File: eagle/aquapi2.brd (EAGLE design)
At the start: 102.5 x 80 mm, 5 parts, among them IC1 RASPBERRY_PI_ZERO_W__V1.3_

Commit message: schemtic added
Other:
- board size 102.5 x 80 mm -> 140.5 x 80 mm
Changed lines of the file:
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@@
 <board>
 <plain>
-<wire x1="0" y1="0" x2="102.54" y2="0" width="0" layer="20"/>
-<wire x1="102.54" y1="0" x2="102.54" y2="80" width="0" layer="20"/>
-<wire x1="102.54" y1="80" x2="0" y2="80" width="0" layer="20"/>
+<wire x1="0" y1="0" x2="140.54" y2="0" width="0" layer="20"/>
+<wire x1="140.54" y1="0" x2="140.54" y2="80" width="0" layer="20"/>
+<wire x1="140.54" y1="80" x2="0" y2="80" width="0" layer="20"/>
 <wire x1="0" y1="80" x2="0" y2="0" width="0" layer="20"/>
 </plain>

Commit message: arudino device lib fixed
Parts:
- added R1, R2, R3, RDIV1: 10k, rcl:R0805
- added RDIV2: 16K, rcl:R0805
- added TR1, TR2, TR3: 10k, discrete:RS-2,5
- moved U$2 29.2 mm to (60.0, 33.0)
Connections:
- net RAW renamed N$4
- new net ARD_RX: IC1.8
- new net ARD_TX: RDIV1.2
- new net N$1: R2.2, TR1.2
- new net N$10: U$2.TX0-1
- new net N$13: U$2.GND
- new net N$14: U$2.GND4
- new net N$15: U$2.DTR
- new net N$2: R1.2, TR2.2
- new net N$3: R3.2, TR3.2
- new net N$5: U$2.A7
- new net N$6: U$2.D9
- new net N$7: U$2.A4
- new net N$8: U$2.TX0
- new net N$9: U$2.RX1
- new net RPI_RX: IC1.10, RDIV1.1, RDIV2.2
- new net THERM1: TR1.1, U$2.A1
- new net THERM2: TR2.1, U$2.A2
- new net THERM3: TR3.1, U$2.A3
- net +5V: now also U$2.VCC1
- net GND: now also R1.1, R2.1, R3.1, RDIV2.1; no longer U$2.GND

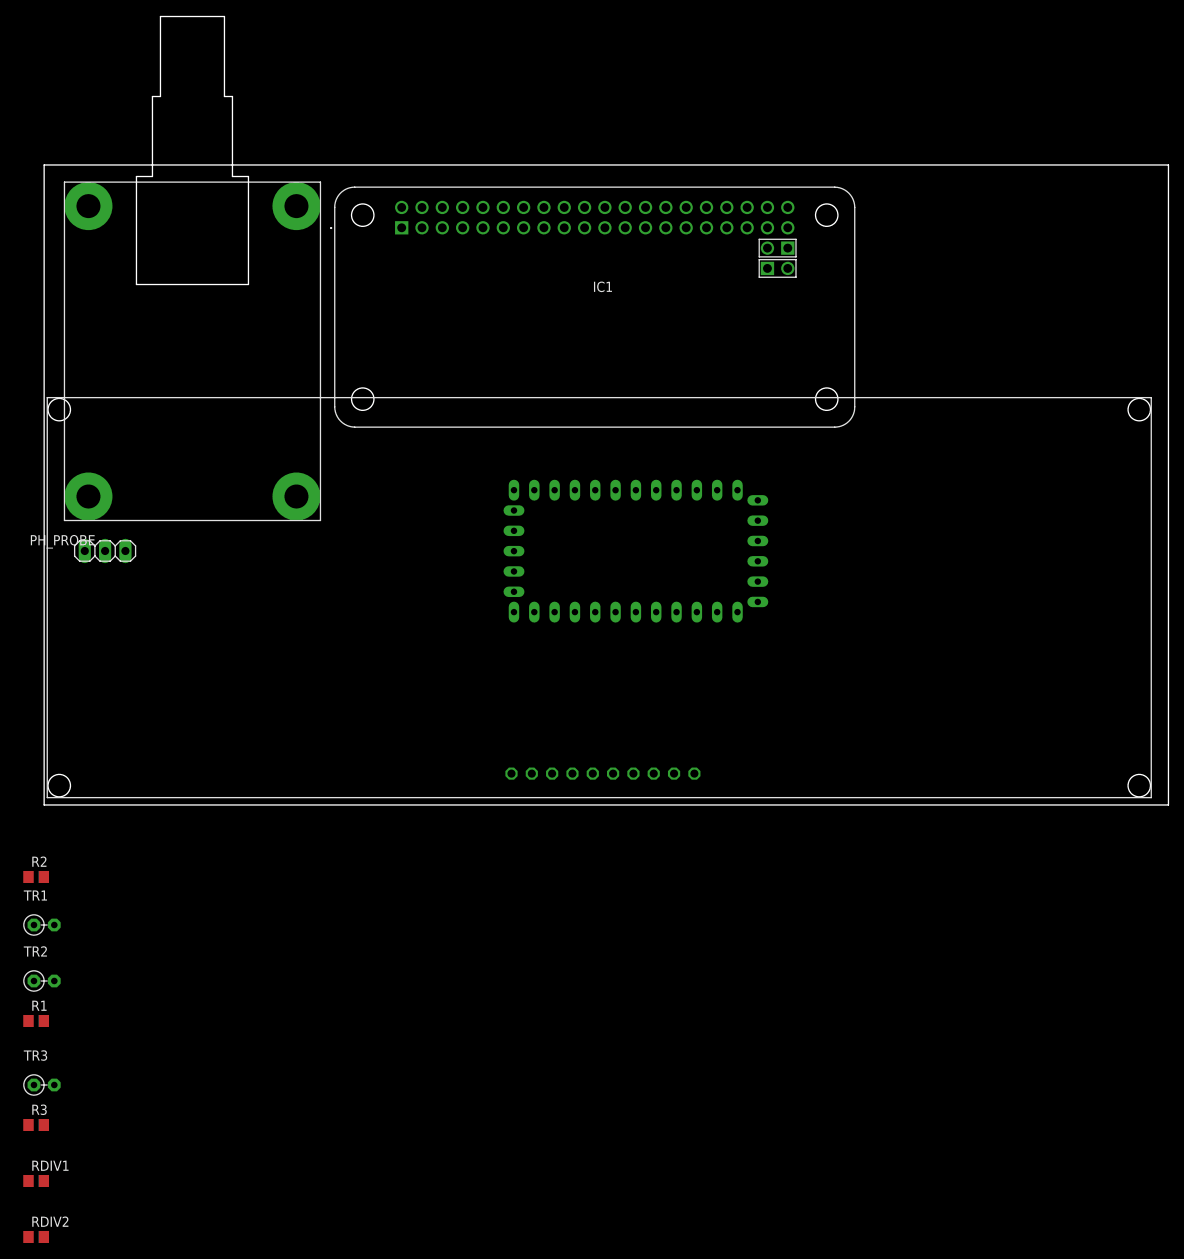
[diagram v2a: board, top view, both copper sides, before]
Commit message: Squashed commit of the following:
commit 7dce77e1b018337bae77b73dfeb2fe2afd6dd7fb
Author: rafal <ravmiecznk@gmail.com>
Date:   Mon Mar 27 18:15:28 2023 +0200

    new constructor from struct

commit 8f6d84a0210c76b2bc0acb519426c939a0a5c33f
Author: rafal <ravmiecznk@gmail.com>
Date:   Mon Mar 27 18:13:10 2023 +0200

    usart draft works

commit a12afc0a744ad612be8265cef467c83d1d3cefab
Author: rafal <ravmiecznk@gmail.com>
Date:   Mon Mar 27 17:49:51 2023 +0200

    schematic fix

commit a0211998f02243aec53f4161e691c0fde81374dd
Author: rafal <ravmiecznk@gmail.com>
Date:   Mon Mar 27 17:49:04 2023 +0200

    Usart constr added

commit c2ed277544ca2c68a412f2a85b5fd8a9273f73a5
Author: rafal <ravmiecznk@gmail.com>
Date:   Sun Mar 26 22:08:04 2023 +0200

    usart and circ buffer added

commit b830d1946cd96a0de6c5bb9a34da8aa961058b17
Author: rafal <ravmiecznk@gmail.com>
Date:   Sun Mar 26 19:27:24 2023 +0200

    avr cpp code added
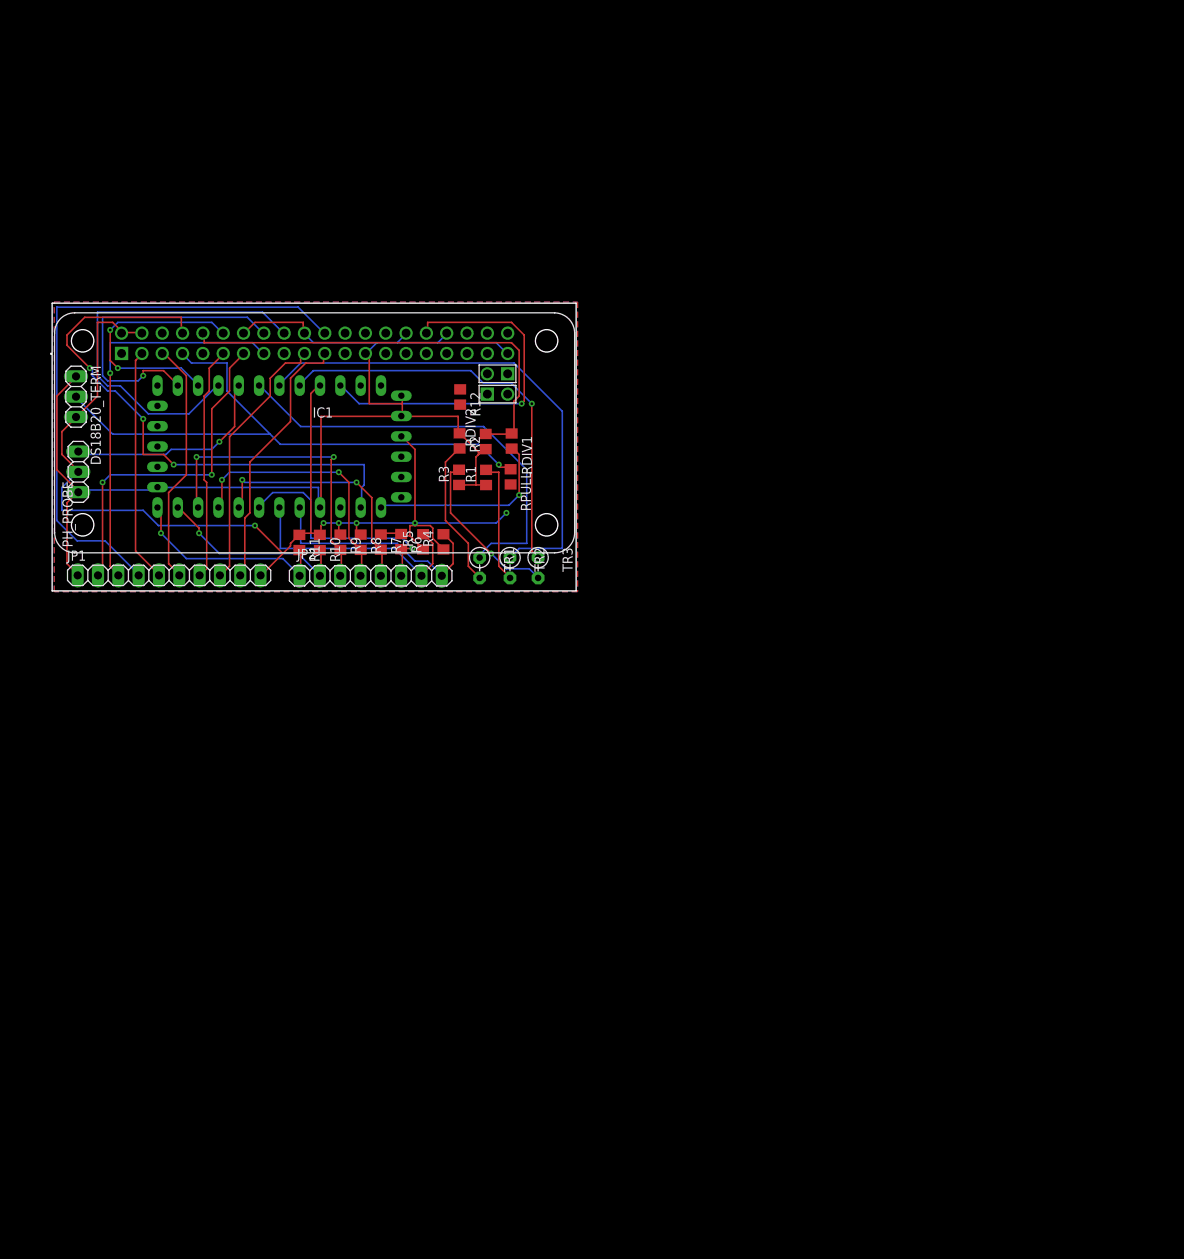
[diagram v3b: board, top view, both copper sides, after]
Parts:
- removed U$1: PH_METER_V2.0, dforbot:PH_METER_V2.0
- removed U$3: RELAY_X8, RELAYx8:RELAY_X8
- added DS18B20_TERM: (no value), pinhead:1X03
- added JP1: (no value), pinhead:1X10
- added JP2: (no value), pinhead:1X08
- added R10, R11, R12, R4, R5, R6, R7, R8, R9, RPULL: 10k, rcl:R0805
- moved RDIV2 114.2 mm to (55.2, 45.4), turned to 90 degrees
- moved RDIV1 109.9 mm to (58.4, 45.5), turned to 270 degrees
- moved R3 96.7 mm to (51.9, 41.0), turned to 90 degrees
- moved TR3 89.4 mm to (61.7, 29.6), turned to 270 degrees
- moved R1 88.2 mm to (55.2, 40.9), turned to 90 degrees
- moved TR2 77.8 mm to (58.2, 29.6), turned to 270 degrees
- moved R2 76.0 mm to (51.9, 45.5), turned to 270 degrees
- moved TR1 70.4 mm to (54.4, 29.6), turned to 270 degrees
- moved U$2 45.8 mm to (15.4, 43.5), flipped to the bottom, turned to 90 degrees
- moved IC1 38.4 mm to (33.6, 46.5)
- moved PH_PROBE 10.4 mm to (4.27, 41.6), turned to 270 degrees
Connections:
- net N$1 renamed WIR3
- net N$2 renamed WIR2
- net N$3 renamed WIR1
- removed net N$14: U$2.GND4
- removed net N$6: U$2.D9
- removed net N$8: U$2.TX0
- removed net N$9: U$2.RX1
- new net +3V3: DS18B20_TERM.3, IC1.1, IC1.17, RPULL.2
- new net DS18B20_OUT: DS18B20_TERM.2, IC1.7, RPULL.1
- new net N$1: U$2.A5
- new net N$2: U$2.A6
- new net N$3: R12.2, U$2.RST
- new net PCINT0: JP2.2, R10.2, U$2.D8
- new net PCINT1: JP2.1, R11.2, U$2.D9
- new net PCINT18: JP2.8, R4.2, U$2.D2
- new net PCINT19: JP2.7, R5.2, U$2.D3
- new net PCINT20: JP2.6, R6.2, U$2.D4
- new net PCINT21: JP2.5, R7.2, U$2.D5
- new net PCINT22: JP2.4, R8.2, U$2.D6
- new net PCINT23: JP2.3, R9.2, U$2.D7
- new net RELAY1: IC1.13, JP1.2
- new net RELAY2: IC1.15, JP1.3
- new net RELAY3: IC1.22, JP1.4
- new net RELAY4: IC1.3, JP1.5
- new net RELAY5: IC1.5, JP1.6
- new net RELAY6: IC1.11, JP1.7
- new net RELAY7: IC1.19, JP1.8
- new net RELAY8: IC1.21, JP1.9
- net +5V: now also JP1.10, R10.1, R11.1, R4.1, R5.1, R6.1, R7.1, R8.1, R9.1; no longer U$3.VCC
- net ARD_RST: now also R12.1; no longer U$2.RST
- net ARD_RX: now also U$2.RX1
- net ARD_TX: now also U$2.TX0
- net GND: now also DS18B20_TERM.1, JP1.1, U$2.GND4; no longer U$3.GND
- net THERM1: now also TR3.1; no longer TR1.1
- net THERM3: now also TR1.1; no longer TR3.1
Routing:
- net GND: track 0.00 -> 157.3 mm
- net +5V: track 0.00 -> 145.5 mm, vias 0 -> 6
- net DS18B20_OUT: track 0.00 -> 75.5 mm, vias 0 -> 1
- net RELAY3: track 0.00 -> 74.6 mm
- net ARD_RX: track 0.00 -> 70.6 mm, vias 0 -> 3
- net THERM2: track 0.00 -> 63.0 mm
- net RPI_RX: track 0.00 -> 55.1 mm
- net THERM1: track 0.00 -> 53.7 mm
- net ARD_SCK: track 0.00 -> 50.9 mm
- net THERM3: track 0.00 -> 50.9 mm, vias 0 -> 1
- net RELAY2: track 0.00 -> 49.2 mm, vias 0 -> 1
- net ARD_RST: track 0.00 -> 46.3 mm, vias 0 -> 1
- net RELAY1: track 0.00 -> 42.7 mm, vias 0 -> 2
- net ARD_MOSI: track 0.00 -> 39.6 mm, vias 0 -> 1
- net PCINT23: track 0.00 -> 39.1 mm, vias 0 -> 2
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- added copper zone on layer 1, net GND
- added copper zone on layer 16, net GND
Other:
- board size 140.5 x 80 mm -> 65.5 x 36 mm
